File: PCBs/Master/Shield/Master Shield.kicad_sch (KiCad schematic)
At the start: 29 parts, among them J1 Power, J2 PWM, J3 Communication

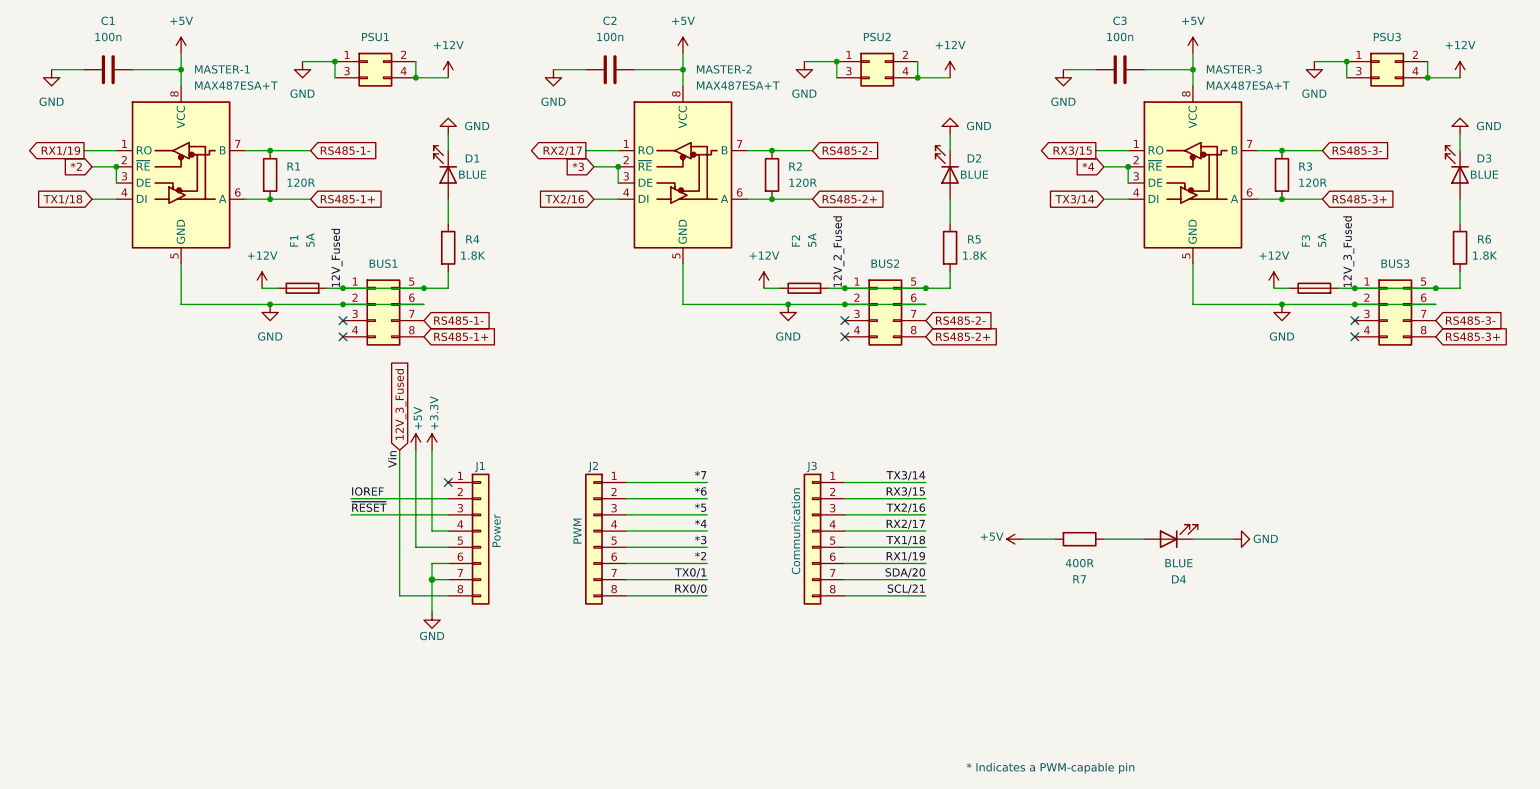
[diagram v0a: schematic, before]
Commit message: Updated micro-fit pinout for more power
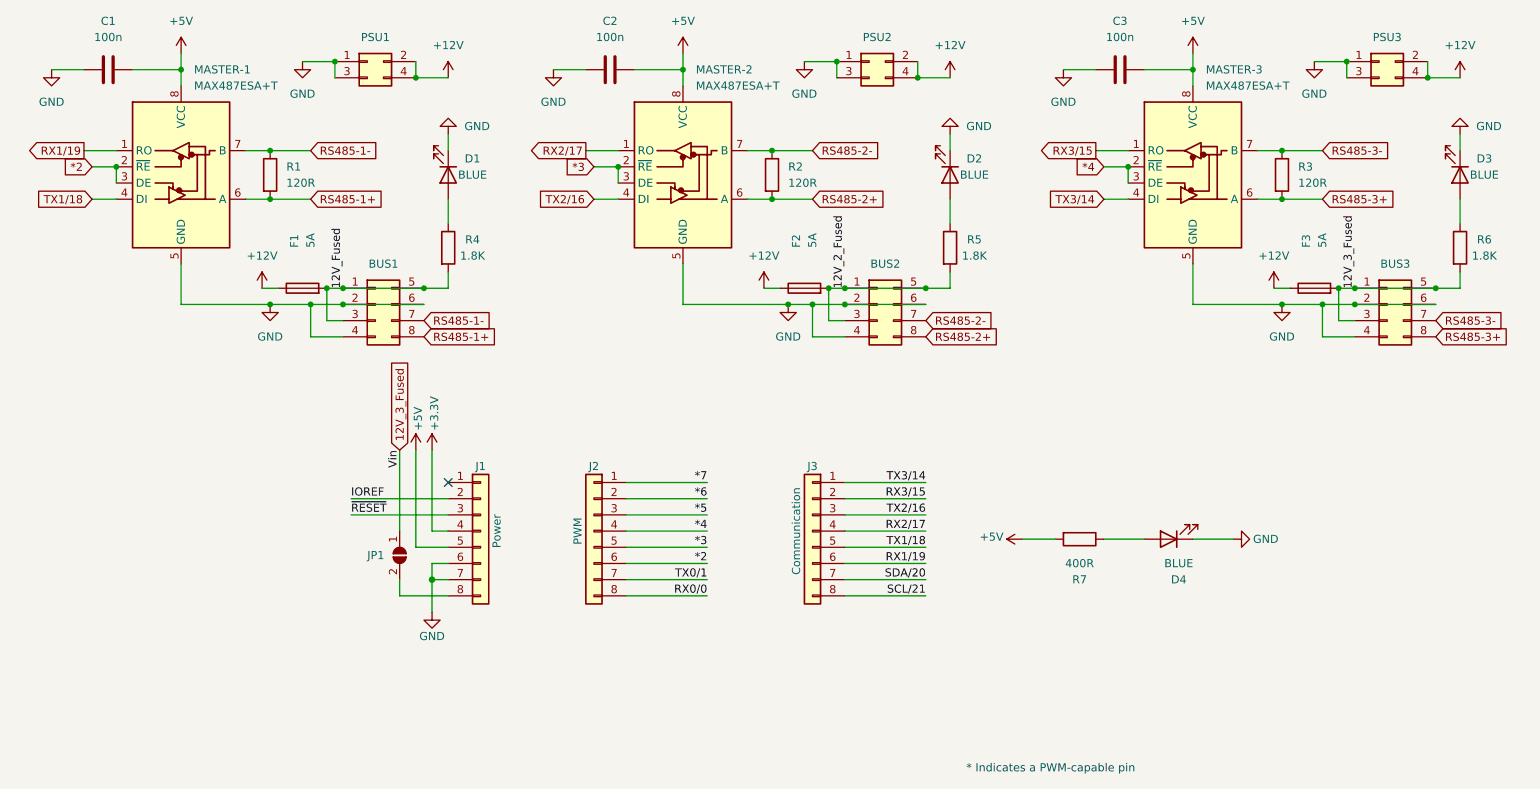
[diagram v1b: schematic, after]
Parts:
- added JP1: SolderJumper_2_Open, Jumper:SolderJumper-2_P1.3mm_Open_RoundedPad1.0x1.5mm, symbol Jumper:SolderJumper_2_Open
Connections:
- net 12V_2_Fused: now also BUS2.3 (Pin_3)
- net 12V_3_Fused: now also BUS3.3 (Pin_3), JP1.1 (A); no longer J1.8 (Pin_8)
- net 12V_Fused: now also BUS1.3 (Pin_3)
- net GND: now also BUS1.4 (Pin_4), BUS2.4 (Pin_4), BUS3.4 (Pin_4)
- new net: J1.8 (Pin_8), JP1.2 (B)
- no-connect marks 7 -> 1
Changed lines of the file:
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@@
   (junction (at 80.01 106.68) (diameter 0) (color 0 0 0 0)
   )
+  (junction (at 74.93 106.68) (diameter 0) (color 0 0 0 0)
+  )
   (junction (at 123.19 85.09) (diameter 0) (color 0 0 0 0)
   )
@@
   (junction (at 68.58 82.55) (diameter 0) (color 0 0 0 0)
   )
+  (junction (at 156.21 104.14) (diameter 0) (color 0 0 0 0)
+  )
+  (junction (at 77.47 104.14) (diameter 0) (color 0 0 0 0)
+  )
   (junction (at 158.75 104.14) (diameter 0) (color 0 0 0 0)
   )
+  (junction (at 233.68 106.68) (diameter 0) (color 0 0 0 0)
+  )
   (junction (at 78.74 68.58) (diameter 0) (color 0 0 0 0)
   )
@@
   (junction (at 251.46 104.14) (diameter 0) (color 0 0 0 0)
   )
+  (junction (at 236.22 104.14) (diameter 0) (color 0 0 0 0)
+  )
   (junction (at 250.19 71.12) (diameter 0) (color 0 0 0 0)
   )
@@
   (junction (at 92.71 104.14) (diameter 0) (color 0 0 0 0)
   )
+  (junction (at 153.67 106.68) (diameter 0) (color 0 0 0 0)
+  )
   (junction (at 213.36 69.85) (diameter 0) (color 0 0 0 0)
   )
   (junction (at 227.33 106.68) (diameter 0) (color 0 0 0 0)
   )
-  (no_connect (at 80.01 109.22))
-  (no_connect (at 158.75 111.76))
-  (no_connect (at 238.76 109.22))
-  (no_connect (at 158.75 109.22))
   (no_connect (at 96.52 134.62))
-  (no_connect (at 80.01 111.76))
-  (no_connect (at 238.76 111.76))
   (wire (pts (xy 251.46 104.14) (xy 255.27 104.14))
     (stroke (width 0) (type default) (color 0 0 0 0))
@@
     (stroke (width 0) (type default) (color 0 0 0 0))
   )
+  (wire (pts (xy 236.22 104.14) (xy 236.22 109.22))
+    (stroke (width 0) (type default) (color 0 0 0 0))
+  )
+  (wire (pts (xy 238.76 111.76) (xy 233.68 111.76))
+    (stroke (width 0) (type default) (color 0 0 0 0))
+  )
   (wire (pts (xy 255.27 90.17) (xy 255.27 93.98))
     (stroke (width 0) (type default) (color 0 0 0 0))
@@
     (stroke (width 0) (type default) (color 0 0 0 0))
   )
+  (wire (pts (xy 153.67 106.68) (xy 158.75 106.68))
+    (stroke (width 0) (type default) (color 0 0 0 0))
+  )
   (wire (pts (xy 125.73 69.85) (xy 133.35 69.85))
     (stroke (width 0) (type default) (color 0 0 0 0))
   )
-  (wire (pts (xy 68.58 106.68) (xy 80.01 106.68))
+  (wire (pts (xy 74.93 111.76) (xy 74.93 106.68))
+    (stroke (width 0) (type default) (color 0 0 0 0))
+  )
+  (wire (pts (xy 88.9 129.54) (xy 88.9 142.24))
+    (stroke (width 0) (type default) (color 0 0 0 0))
+  )
+  (wire (pts (xy 68.58 106.68) (xy 74.93 106.68))
     (stroke (width 0) (type default) (color 0 0 0 0))
   )
@@
     (stroke (width 0) (type default) (color 0 0 0 0))
   )
+  (wire (pts (xy 153.67 111.76) (xy 153.67 106.68))
+    (stroke (width 0) (type default) (color 0 0 0 0))
+  )
   (wire (pts (xy 133.35 69.85) (xy 133.35 72.39))
     (stroke (width 0) (type default) (color 0 0 0 0))
@@
     (stroke (width 0) (type solid) (color 0 0 0 0))
   )
+  (wire (pts (xy 156.21 104.14) (xy 156.21 109.22))
+    (stroke (width 0) (type default) (color 0 0 0 0))
+  )
   (wire (pts (xy 91.44 144.78) (xy 96.52 144.78))
     (stroke (width 0) (type solid) (color 0 0 0 0))
@@
     (stroke (width 0) (type default) (color 0 0 0 0))
   )
-  (wire (pts (xy 227.33 106.68) (xy 238.76 106.68))
+  (wire (pts (xy 227.33 106.68) (xy 233.68 106.68))
     (stroke (width 0) (type default) (color 0 0 0 0))
   )
@@
     (stroke (width 0) (type solid) (color 0 0 0 0))
   )
+  (wire (pts (xy 77.47 109.22) (xy 80.01 109.22))
+    (stroke (width 0) (type default) (color 0 0 0 0))
+  )
   (wire (pts (xy 143.51 90.17) (xy 147.32 90.17))
     (stroke (width 0) (type default) (color 0 0 0 0))
@@
     (stroke (width 0) (type default) (color 0 0 0 0))
   )
+  (wire (pts (xy 236.22 109.22) (xy 238.76 109.22))
+    (stroke (width 0) (type default) (color 0 0 0 0))
+  )
   (wire (pts (xy 158.75 152.4) (xy 171.45 152.4))
     (stroke (width 0) (type solid) (color 0 0 0 0))
@@
     (stroke (width 0) (type default) (color 0 0 0 0))
   )
+  (wire (pts (xy 88.9 149.86) (xy 88.9 152.4))
+    (stroke (width 0) (type default) (color 0 0 0 0))
+  )
   (wire (pts (xy 54.61 100.33) (xy 54.61 106.68))
     (stroke (width 0) (type default) (color 0 0 0 0))
@@
     (stroke (width 0) (type default) (color 0 0 0 0))
   )
-  (wire (pts (xy 149.86 106.68) (xy 158.75 106.68))
+  (wire (pts (xy 158.75 111.76) (xy 153.67 111.76))
+    (stroke (width 0) (type default) (color 0 0 0 0))
+  )
+  (wire (pts (xy 149.86 106.68) (xy 153.67 106.68))
     (stroke (width 0) (type default) (color 0 0 0 0))
   )
@@
     (stroke (width 0) (type solid) (color 0 0 0 0))
   )
+  (wire (pts (xy 80.01 111.76) (xy 74.93 111.76))
+    (stroke (width 0) (type default) (color 0 0 0 0))
+  )
   (wire (pts (xy 227.33 90.17) (xy 233.68 90.17))
     (stroke (width 0) (type default) (color 0 0 0 0))
@@
     (stroke (width 0) (type default) (color 0 0 0 0))
   )
+  (wire (pts (xy 156.21 109.22) (xy 158.75 109.22))
+    (stroke (width 0) (type default) (color 0 0 0 0))
+  )
   (wire (pts (xy 124.46 139.7) (xy 137.16 139.7))
     (stroke (width 0) (type solid) (color 0 0 0 0))
@@
     (stroke (width 0) (type default) (color 0 0 0 0))
   )
+  (wire (pts (xy 233.68 106.68) (xy 238.76 106.68))
+    (stroke (width 0) (type default) (color 0 0 0 0))
+  )
   (wire (pts (xy 158.75 149.86) (xy 171.45 149.86))
     (stroke (width 0) (type solid) (color 0 0 0 0))
@@
     (stroke (width 0) (type default) (color 0 0 0 0))
   )
+  (wire (pts (xy 77.47 104.14) (xy 77.47 109.22))
+    (stroke (width 0) (type default) (color 0 0 0 0))
+  )
+  (wire (pts (xy 74.93 106.68) (xy 80.01 106.68))
+    (stroke (width 0) (type default) (color 0 0 0 0))
+  )
   (wire (pts (xy 124.46 149.86) (xy 137.16 149.86))
     (stroke (width 0) (type solid) (color 0 0 0 0))
   )
-  (wire (pts (xy 88.9 152.4) (xy 88.9 129.54))
-    (stroke (width 0) (type solid) (color 0 0 0 0))
+  (wire (pts (xy 233.68 111.76) (xy 233.68 106.68))
+    (stroke (width 0) (type default) (color 0 0 0 0))
   )
   (wire (pts (xy 156.21 104.14) (xy 158.75 104.14))
@@
     (pin "1")
   )
+  (symbol (lib_id "Jumper:SolderJumper_2_Open") (at 88.9 146.05 270) (unit 1)
+    (in_bom yes) (on_board yes)
+    (property "Reference" "JP1" (id 0) (at 83.82 146.05 90)
+      (effects (font (size 1.27 1.27)) (justify left))
+    )
+    (property "Value" "SolderJumper_2_Open" (id 1) (at 91.44 147.3199 90)
+      (effects (font (size 1.27 1.27)) (justify left) hide)
+    )
+    (property "Footprint" "Jumper:SolderJumper-2_P1.3mm_Open_RoundedPad1.0x1.5mm" (id 2) (at 88.9 146.05 0)
+      (effects (font (size 1.27 1.27)) hide)
+    )
+    (property "Datasheet" "~" (id 3) (at 88.9 146.05 0)
+      (effects (font (size 1.27 1.27)) hide)
+    )
+    (pin "1")
+    (pin "2")
+  )
   (symbol (lib_id "Device:C") (at 121.92 69.85 90) (unit 1)
     (in_bom yes) (on_board yes) (fields_autoplaced)
@@
       (reference "J3") (unit 1) (value "Communication") (footprint "Connector_PinHeader_2.54mm:PinHeader_1x08_P2.54mm_Vertical")
     )
+    (path "/a6746be1-5856-46c9-8ceb-9ffdcf28f39b"
+      (reference "JP1") (unit 1) (value "SolderJumper_2_Open") (footprint "Jumper:SolderJumper-2_P1.3mm_Open_RoundedPad1.0x1.5mm")
+    )
     (path "/c0c882df-c766-4934-bdff-dcff796a7bfe"
